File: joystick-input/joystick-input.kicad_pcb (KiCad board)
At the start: 2 copper layers, 53.3 x 39.4 mm, 11 parts

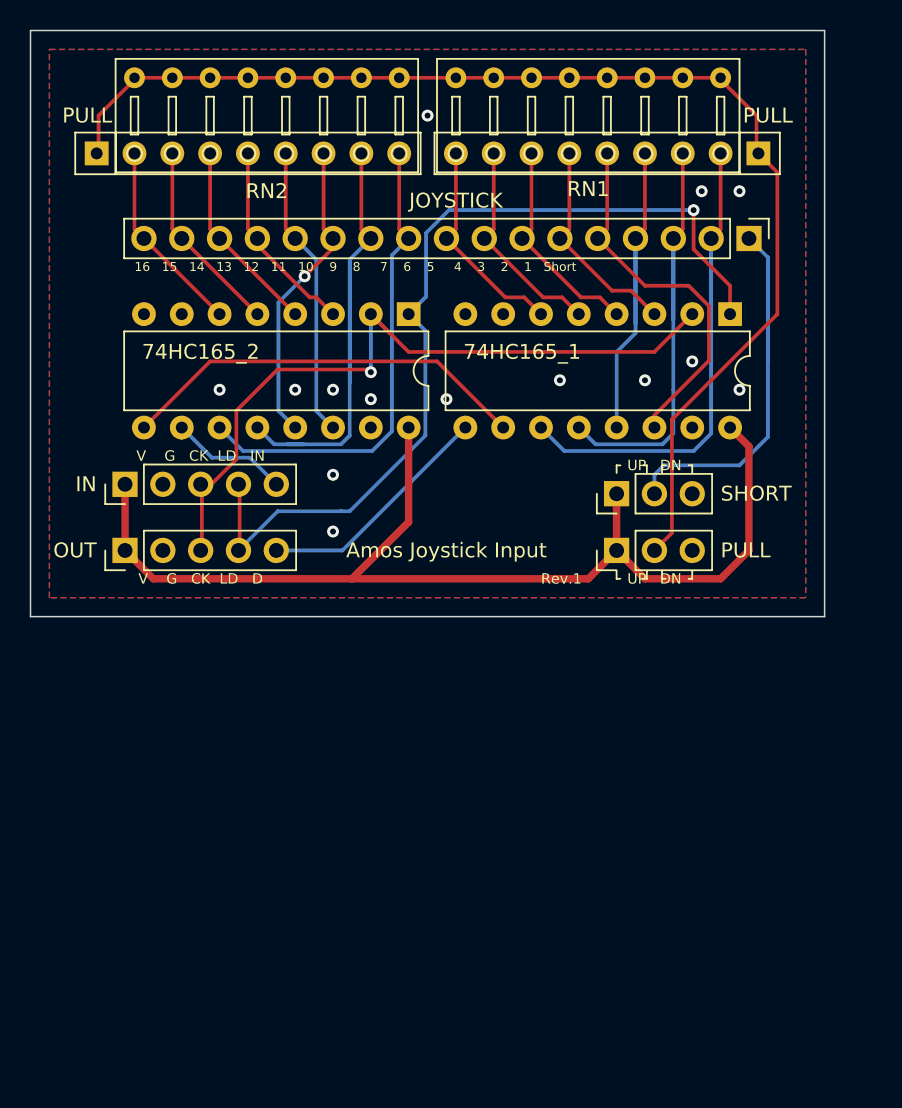
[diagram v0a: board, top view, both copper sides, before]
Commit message: * esp-debug-adapter : 트레이스 개선 * joystick-input : SMD로 변경
Signed-off-by: Ju, Gyeong-min <jcmh74@gmail.com>
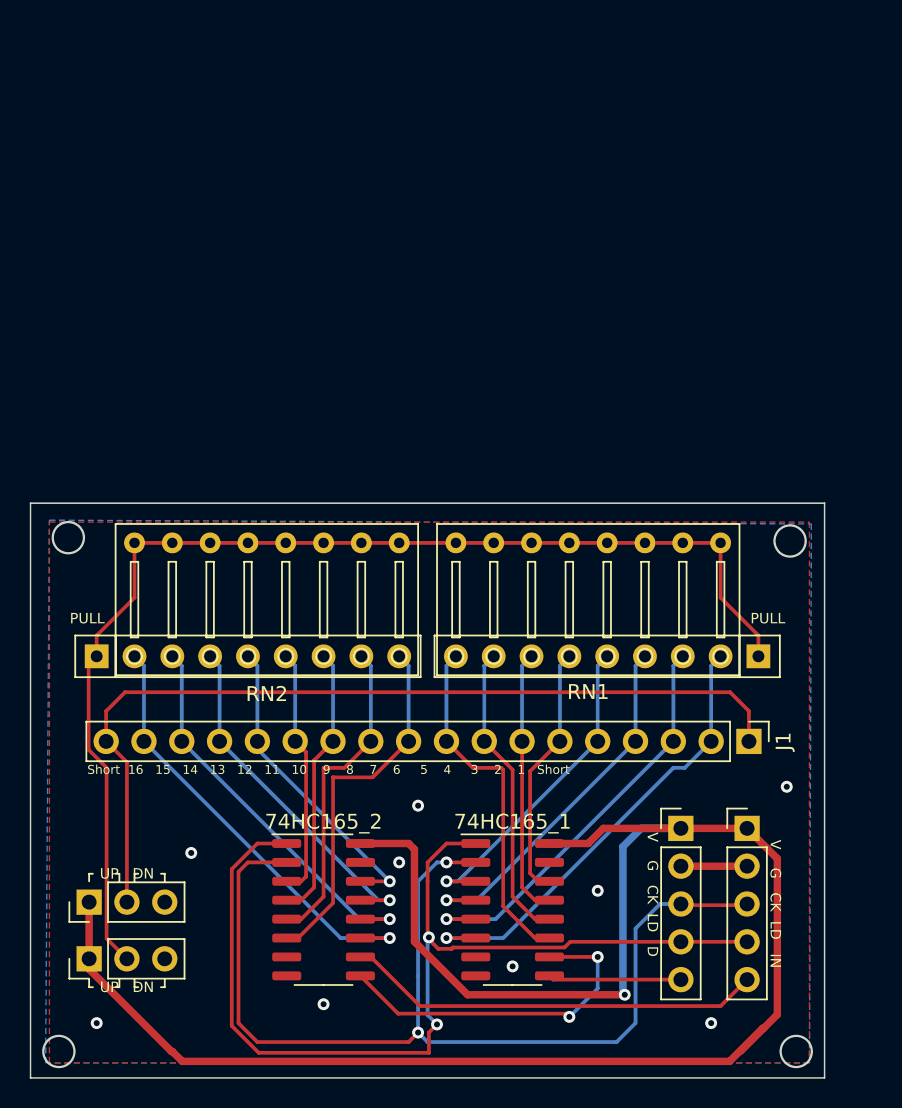
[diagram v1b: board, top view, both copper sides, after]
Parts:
- removed IN, OUT: Conn_01x05_Male, Connector_PinHeader_2.54mm:PinHeader_1x05_P2.54mm_Vertical
- removed JOYSTICK: Conn_01x17_Male, Connector_PinHeader_2.54mm:PinHeader_1x17_P2.54mm_Vertical
- removed PULL, SHORT: Conn_01x03_Male, Connector_PinHeader_2.54mm:PinHeader_1x03_P2.54mm_Vertical
- added IN1: Conn_01x05_Male, Connector_PinHeader_2.54mm:PinHeader_1x05_P2.54mm_Vertical, F.Cu at (159.9, 84.1)
- added J1: Conn_01x18_Male, Connector_PinHeader_2.54mm:PinHeader_1x18_P2.54mm_Vertical, F.Cu at (160.0, 78.2)
- added OUT1: Conn_01x05_Male, Connector_PinHeader_2.54mm:PinHeader_1x05_P2.54mm_Vertical, F.Cu at (155.4, 84.1)
- added PULL1: Conn_01x03_Male, Connector_PinHeader_2.54mm:PinHeader_1x03_P2.54mm_Vertical, F.Cu at (115.7, 92.8)
- added SHORT1: Conn_01x03_Male, Connector_PinHeader_2.54mm:PinHeader_1x03_P2.54mm_Vertical, F.Cu at (115.7, 89.0)
- 74HC165_1, 74HC165_2: footprint Package_DIP:DIP-16_W7.62mm -> Package_SO:SOIC-16_3.9x9.9mm_P1.27mm
- moved 74HC165_1 42.6 mm to (144.1, 89.5), turned to 0 degrees
- moved 74HC165_2 40.4 mm to (131.4, 89.5), turned to 0 degrees
- moved RN1 33.8 mm to (160.7, 72.5)
- moved RN2 33.8 mm to (116.2, 72.5)
- moved H1 31.6 mm to (136.5, 64.9), turned to 270 degrees
- moved H2 31.6 mm to (158.1, 64.9), turned to 270 degrees
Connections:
- 74HC165_1 pad 11: /C_UP -> /C_B
- 74HC165_1 pad 12: /C_DOWN -> /C_A
- 74HC165_1 pad 13: /C_LEFT -> /C_SELECT
- 74HC165_1 pad 14: /C_RIGHT -> /C_START
- 74HC165_1 pad 3: /C_START -> /C_RIGHT
- 74HC165_1 pad 4: /C_SELECT -> /C_LEFT
- 74HC165_1 pad 5: /C_A -> /C_DOWN
- 74HC165_1 pad 6: /C_B -> /C_UP
- 74HC165_2 pad 11: /C_X -> /C_EX4
- 74HC165_2 pad 12: /C_Y -> /C_EX3
- 74HC165_2 pad 13: /C_L -> /C_EX2
- 74HC165_2 pad 14: /C_R -> /C_EX1
- 74HC165_2 pad 3: /C_EX1 -> /C_R
- 74HC165_2 pad 4: /C_EX2 -> /C_L
- 74HC165_2 pad 5: /C_EX3 -> /C_Y
- 74HC165_2 pad 6: /C_EX4 -> /C_X
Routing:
- net VCC: track 73.8 -> 123.8 mm, vias 0 -> 1
- net /C_SHORT: track 30.8 -> 59.7 mm
- net /CLK: track 50.0 -> 71.2 mm, vias 1 -> 2
- net /D_IN: track 8.64 -> 28.1 mm
- net /C_EX4: track 13.2 -> 29.9 mm, vias 0 -> 1
- net /C_Y: track 36.0 -> 21.6 mm
- net /C_EX3: track 13.2 -> 26.9 mm, vias 0 -> 1
- net /C_EX2: track 13.2 -> 23.8 mm, vias 0 -> 1
- net /C_B: track 14.4 -> 23.7 mm
- net /C_EX1: track 13.4 -> 21.0 mm, vias 0 -> 1
- net /C_UP: track 38.8 -> 31.2 mm, vias 0 -> 1
- net /C_X: track 32.2 -> 24.6 mm
- net /LOAD: track 60.7 -> 68.3 mm, vias 1 -> 2
- net /D_OUT: track 16.1 -> 8.93 mm
- net /C_A: track 14.4 -> 20.3 mm
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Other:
- board size 53.3 x 39.4 mm -> 53.3 x 38.6 mm
- board text added: "Rev.2"
- board text added: "Short 16 15 14 13 12 11 10 9 8 7 6 5 4 3 2 1 Short"
- board text removed: "16 15 14 13 12 11 10 9 8 7 6 5 4 3 2 1 Short"
- board text removed: "Rev.1"

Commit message: joystick 보드 원복
Signed-off-by: Ju, Gyeong-min <jcmh74@gmail.com>
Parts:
- removed IN1, OUT1: Conn_01x05_Male, Connector_PinHeader_2.54mm:PinHeader_1x05_P2.54mm_Vertical
- removed J1: Conn_01x18_Male, Connector_PinHeader_2.54mm:PinHeader_1x18_P2.54mm_Vertical
- removed PULL1, SHORT1: Conn_01x03_Male, Connector_PinHeader_2.54mm:PinHeader_1x03_P2.54mm_Vertical
- added IN: Conn_01x05_Male, Connector_PinHeader_2.54mm:PinHeader_1x05_P2.54mm_Vertical, F.Cu at (118.1, 61.0)
- added JOYSTICK: Conn_01x17_Male, Connector_PinHeader_2.54mm:PinHeader_1x17_P2.54mm_Vertical, F.Cu at (160.0, 44.5)
- added OUT: Conn_01x05_Male, Connector_PinHeader_2.54mm:PinHeader_1x05_P2.54mm_Vertical, F.Cu at (118.1, 65.4)
- added PULL: Conn_01x03_Male, Connector_PinHeader_2.54mm:PinHeader_1x03_P2.54mm_Vertical, F.Cu at (151.1, 65.4)
- added SHORT: Conn_01x03_Male, Connector_PinHeader_2.54mm:PinHeader_1x03_P2.54mm_Vertical, F.Cu at (151.1, 61.6)
- 74HC165_1, 74HC165_2: footprint Package_SO:SOIC-16_3.9x9.9mm_P1.27mm -> Package_DIP:DIP-16_W7.62mm
- moved 74HC165_1 42.6 mm to (158.8, 49.5), turned to 270 degrees
- moved 74HC165_2 40.4 mm to (137.2, 49.5), turned to 270 degrees
- moved RN1 33.8 mm to (160.7, 38.7)
- moved RN2 33.8 mm to (116.2, 38.7)
- moved H1 31.6 mm to (118.7, 38.7), turned to 90 degrees
- moved H2 31.6 mm to (140.3, 38.7), turned to 90 degrees
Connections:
- 74HC165_1 pad 11: /C_B -> /C_UP
- 74HC165_1 pad 12: /C_A -> /C_DOWN
- 74HC165_1 pad 13: /C_SELECT -> /C_LEFT
- 74HC165_1 pad 14: /C_START -> /C_RIGHT
- 74HC165_1 pad 3: /C_RIGHT -> /C_START
- 74HC165_1 pad 4: /C_LEFT -> /C_SELECT
- 74HC165_1 pad 5: /C_DOWN -> /C_A
- 74HC165_1 pad 6: /C_UP -> /C_B
- 74HC165_2 pad 11: /C_EX4 -> /C_X
- 74HC165_2 pad 12: /C_EX3 -> /C_Y
- 74HC165_2 pad 13: /C_EX2 -> /C_L
- 74HC165_2 pad 14: /C_EX1 -> /C_R
- 74HC165_2 pad 3: /C_R -> /C_EX1
- 74HC165_2 pad 4: /C_L -> /C_EX2
- 74HC165_2 pad 5: /C_Y -> /C_EX3
- 74HC165_2 pad 6: /C_X -> /C_EX4
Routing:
- net VCC: track 123.8 -> 73.8 mm, vias 1 -> 0
- net /C_SHORT: track 59.7 -> 30.8 mm
- net /CLK: track 71.2 -> 50.0 mm, vias 2 -> 1
- net /D_IN: track 28.1 -> 8.64 mm
- net /C_EX4: track 29.9 -> 13.2 mm, vias 1 -> 0
- net /C_Y: track 21.6 -> 36.0 mm
- net /C_EX3: track 26.9 -> 13.2 mm, vias 1 -> 0
- net /C_EX2: track 23.8 -> 13.2 mm, vias 1 -> 0
- net /C_B: track 23.7 -> 14.4 mm
- net /C_EX1: track 21.0 -> 13.4 mm, vias 1 -> 0
- net /C_UP: track 31.2 -> 38.8 mm, vias 1 -> 0
- net /C_X: track 24.6 -> 32.2 mm
- net /LOAD: track 68.3 -> 60.7 mm, vias 2 -> 1
- net /D_OUT: track 8.93 -> 16.1 mm
- net /C_A: track 20.3 -> 14.4 mm
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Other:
- board size 53.3 x 38.6 mm -> 53.3 x 39.4 mm
- board text added: "16 15 14 13 12 11 10 9 8 7 6 5 4 3 2 1 Short"
- board text added: "Rev.1"
- board text removed: "Rev.2"
- board text removed: "Short 16 15 14 13 12 11 10 9 8 7 6 5 4 3 2 1 Short"
